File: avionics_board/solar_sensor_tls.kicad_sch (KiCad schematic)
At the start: 5 parts, among them J10 Conn_01x08

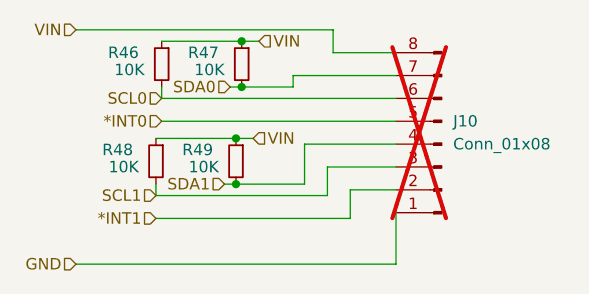
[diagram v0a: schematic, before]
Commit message: add headers for ACS and sun sensors
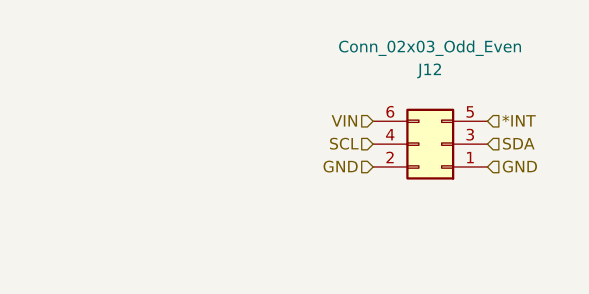
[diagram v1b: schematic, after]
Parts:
- removed R46, R47, R48, R49: 10K, Resistor_SMD:R_0402_1005Metric_Pad0.72x0.64mm_HandSolder, symbol Device:R_Small
- J12: renamed from J10; value Conn_01x08 -> Conn_02x03_Odd_Even; footprint Connector_PinHeader_2.54mm:PinHeader_1x08_P2.54mm_Vertical -> Common:SAMTEC-CLP-103-02-X-DH; symbol Connector:Conn_01x08_Pin -> Connector_Generic:Conn_02x03_Odd_Even; now fitted
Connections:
- net *INT1 is gone; now on net GND: J12.2 (Pin_2)
- net SCL0 is gone; now on net VIN: J12.6 (Pin_6)
- net VIN: no longer J12.8 (Pin_8)
- net *INT0 renamed *INT
- net SCL1 renamed SDA
- removed net SDA0: J12.7 (Pin_7)
- net SDA1 renamed SCL
